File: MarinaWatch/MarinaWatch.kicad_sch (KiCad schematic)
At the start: 2 parts, among them J1 USB_C_Receptacle_USB2.0_16P, U1 ESP32-S3-WROOM-1

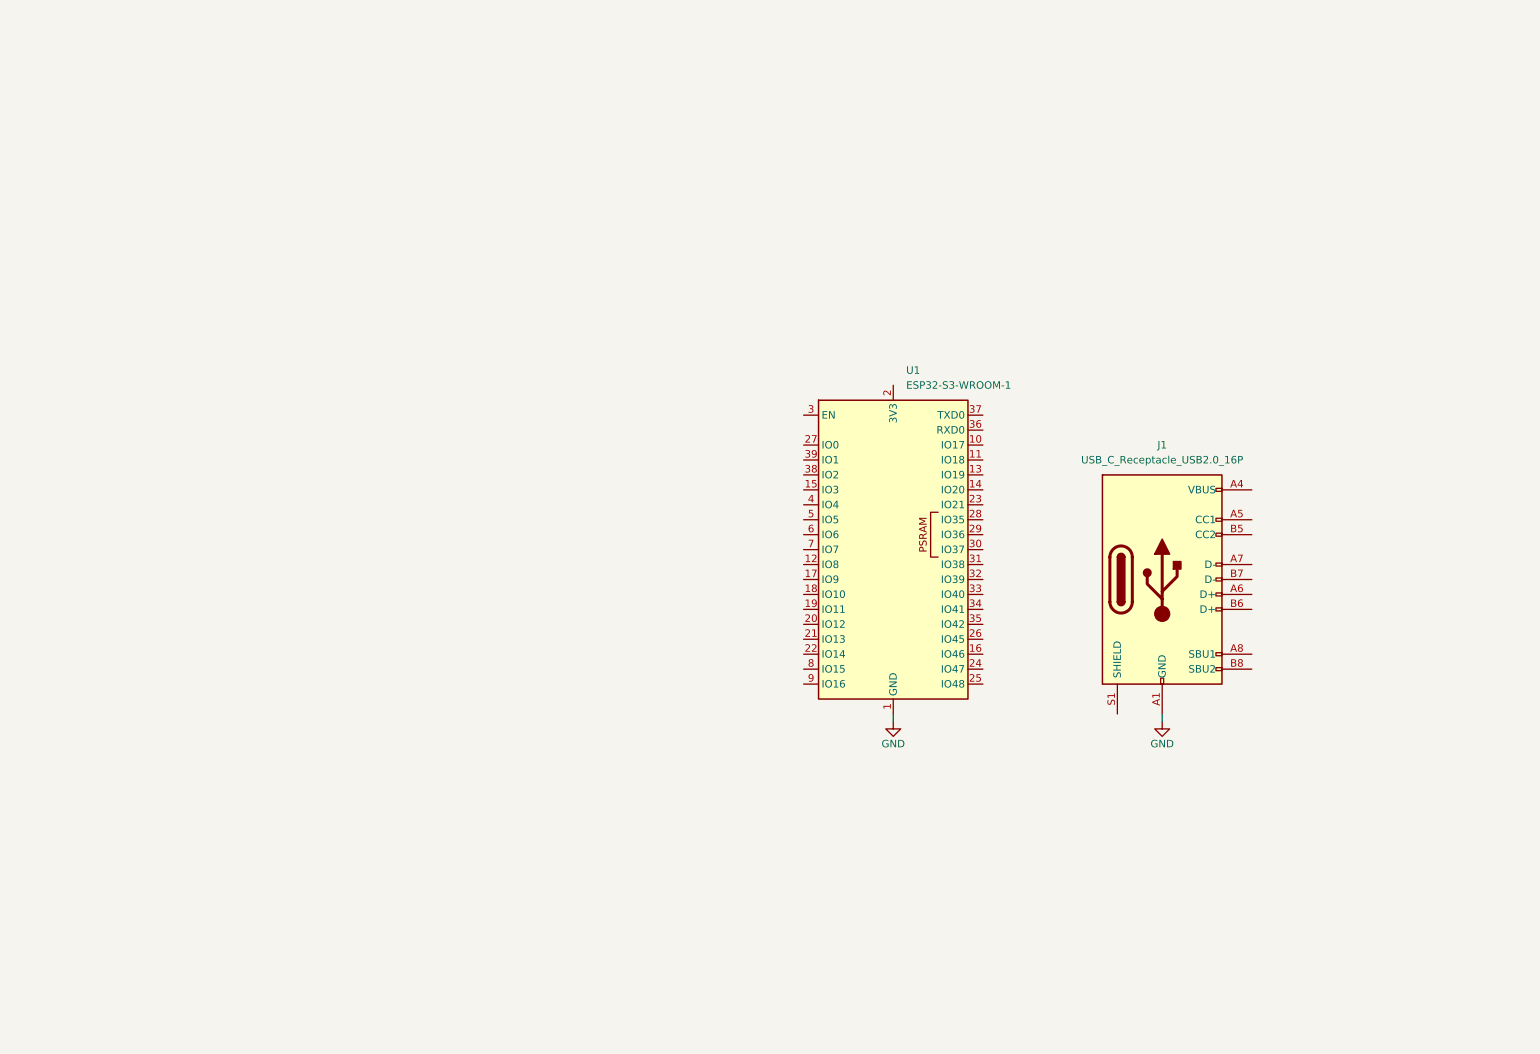
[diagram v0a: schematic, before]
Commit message: Finished USB hardware. Started power supply.
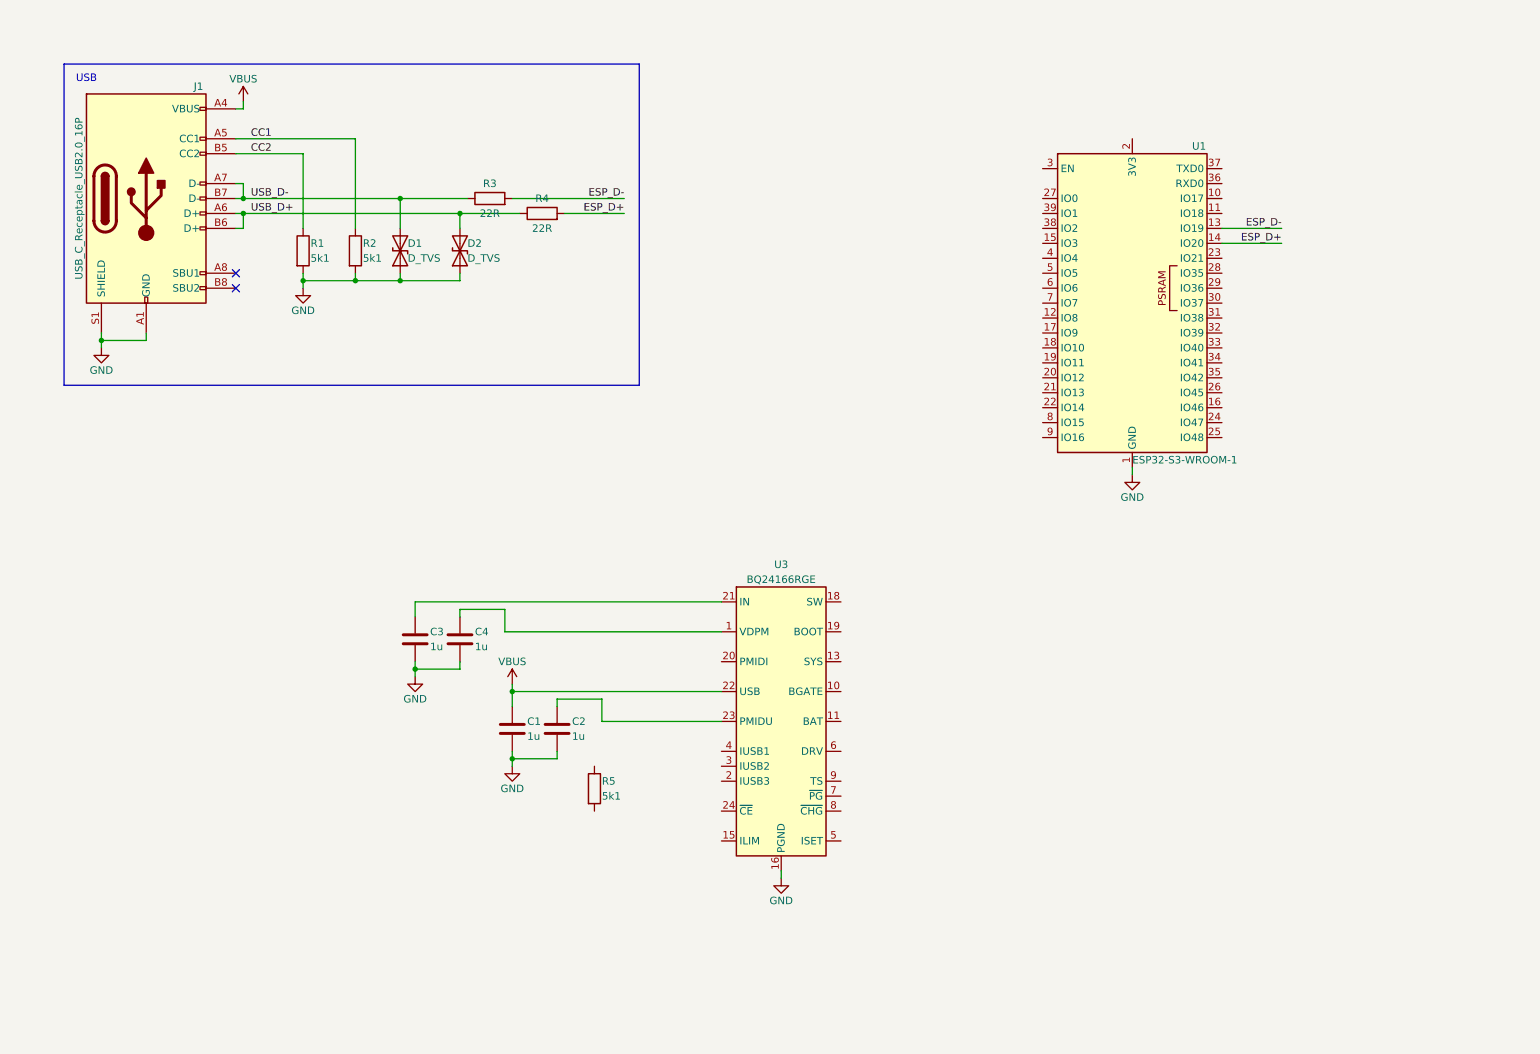
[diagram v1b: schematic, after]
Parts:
- added C1, C2, C3, C4: 1u, Capacitor_SMD:C_0603_1608Metric_Pad1.08x0.95mm_HandSolder, symbol Device:C
- added D1, D2: D_TVS, Fuse:Fuse_0603_1608Metric_Pad1.05x0.95mm_HandSolder, symbol Device:D_TVS
- added R1, R2, R5: 5k1, Resistor_SMD:R_0603_1608Metric_Pad0.98x0.95mm_HandSolder, symbol Device:R
- added R3, R4: 22R, Resistor_SMD:R_0603_1608Metric_Pad0.98x0.95mm_HandSolder, symbol Device:R
- added U3: BQ24166RGE, Package_DFN_QFN:Texas_RGE0024H_VQFN-24-1EP_4x4mm_P0.5mm_EP2.7x2.7mm, symbol Battery_Management:BQ24166RGE
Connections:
- net GND: now also J1.S1 (SHIELD), C1.2, C2.2, C3.2, C4.2, D1.1 (A1), D2.1 (A1), R1.2, R2.2, U3.16 (PGND), U3.17 (PGND), U3.25 (PGND)
- net VBUS: now reaches J1.A4 (VBUS), J1.A9 (VBUS), J1.B4 (VBUS), J1.B9 (VBUS)
- net VBUS: now also C1.1, U3.22 (USB)
- net CC1: now reaches J1.A5 (CC1)
- net CC1: now also R2.1
- net USB_D+: now reaches J1.A6 (D+)
- net USB_D+: now also J1.B6 (D+), D2.2 (A2), R4.1
- net USB_D-: now reaches J1.A7 (D-)
- net USB_D-: now also J1.B7 (D-), D1.2 (A2), R3.1
- net CC2: now reaches J1.B5 (CC2)
- net CC2: now also R1.1
- net ESP_D-: now reaches U1.13 (IO19)
- net ESP_D-: now also R3.2
- net ESP_D+: now reaches U1.14 (IO20)
- net ESP_D+: now also R4.2
- new net: C4.1, U3.1 (VDPM)
- new net: U3.11 (BAT), U3.12 (BAT)
- new net: U3.13 (SYS), U3.14 (SYS)
- new net: C3.1, U3.21 (IN)
- new net: C2.1, U3.23 (PMIDU)
- no-connect marks 0 -> 2
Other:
- note added: "USB"
- moved on the sheet: J1, U1

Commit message: Structure power supply chain
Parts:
- removed C4: 1u, Capacitor_SMD:C_0603_1608Metric_Pad1.08x0.95mm_HandSolder, symbol Device:C
- added BT1: Battery_Cell, symbol Device:Battery_Cell
- added C10, C11, C12: 10u, Capacitor_SMD:C_0603_1608Metric_Pad1.08x0.95mm_HandSolder, symbol Device:C
- added C5, C6, C7: 1u, Capacitor_SMD:C_0603_1608Metric_Pad1.08x0.95mm_HandSolder, symbol Device:C
- added C8: 4u7, Capacitor_SMD:C_0603_1608Metric_Pad1.08x0.95mm_HandSolder, symbol Device:C
- added C9: 100n, Capacitor_SMD:C_0603_1608Metric_Pad1.08x0.95mm_HandSolder, symbol Device:C
- added IC1: 2609011181000, Lund Formula Student:2609011181000, symbol Lund Formula Student:2609011181000
- added J2: Screw_Terminal_01x02, TerminalBlock_Phoenix:TerminalBlock_Phoenix_MKDS-3-2-5.08_1x02_P5.08mm_Horizontal, symbol Connector:Screw_Terminal_01x02
- added J3: Screw_Terminal_01x02, symbol Connector:Screw_Terminal_01x02
- added J4: Screw_Terminal_01x03, symbol Connector:Screw_Terminal_01x03
- added L1, L2: 2u2, Inductor_SMD_Wurth:L_Wurth_WE-LQSH-4020, symbol Device:L
- added R10: 1k, Resistor_SMD:R_0603_1608Metric_Pad0.98x0.95mm_HandSolder, symbol Device:R
- added R11: 100R, Resistor_SMD:R_0603_1608Metric_Pad0.98x0.95mm_HandSolder, symbol Device:R
- added R12, R6, R7, R8, R9: 10k, Resistor_SMD:R_0603_1608Metric_Pad0.98x0.95mm_HandSolder, symbol Device:R
- added R13: 27k, Resistor_SMD:R_0603_1608Metric_Pad0.98x0.95mm_HandSolder, symbol Device:R
- added TP1, TP2, TP3, TP4, TP5: TestPoint, TestPoint:TestPoint_Pad_D2.0mm, symbol Connector:TestPoint
- added U2: TPS63001, Package_SON:Texas_DRC0010J_ThermalVias, symbol Regulator_Switching:TPS63001
- R5: value 5k1 -> 10k
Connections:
- net GND: now also BT1.2 (-), C10.2, C11.2, C12.2, C5.2, C7.2, C8.2, C9.2, IC1.2 (GND_1), IC1.23 (GND_2), J2.2 (Pin_2), J3.2 (Pin_2), J4.3 (Pin_3), R10.2, R12.2, R6.2, R7.2, R8.2, R9.2, U2.11 (PGND), U2.3 (PGND), U2.9 (GND)
- net VBUS: now also R5.1, TP1.1
- net IUSB1: now reaches R5.2
- net IUSB1: now also U3.4 (IUSB1)
- net VDPM: now reaches U3.1 (VDPM)
- net VDPM: now also R12.1, R13.2
- net +BATT: now reaches U3.11 (BAT), U3.12 (BAT)
- net +BATT: now also BT1.1 (+), TP3.1
- net VCC: now reaches U3.13 (SYS), U3.14 (SYS)
- net VCC: now also C10.1, C7.1, L1.2, R11.1, TP4.1, U2.5 (VIN)
- net ILIM: now reaches U3.15 (ILIM)
- net ILIM: now also R8.1
- net SW: now reaches U3.18 (SW)
- net SW: now also C6.1, L1.1
- net BOOT: now reaches U3.19 (BOOT)
- net BOOT: now also C6.2
- net IUSB3: now reaches U3.2 (IUSB3)
- net IUSB3: now also R6.1
- net PMIDI: now reaches U3.20 (PMIDI)
- net PMIDI: now also C8.1
- net VDD: now reaches C3.1, U3.21 (IN)
- net VDD: now also J2.1 (Pin_1), R13.1, TP2.1
- net PMIDU: now reaches C2.1, U3.23 (PMIDU)
- net CE: now reaches U3.24 (~{CE})
- net CE: now also R9.1
- net IUSB2: now reaches U3.3 (IUSB2)
- net IUSB2: now also R7.1
- net ISET: now reaches U3.5 (ISET)
- net ISET: now also R10.1
- net DRV: now reaches U3.6 (DRV)
- net DRV: now also C5.1
- net +3.3V: now reaches U1.2 (3V3)
- net +3.3V: now also C11.1, C12.1, IC1.3 (VCC), J4.1 (Pin_1), TP5.1, U2.1 (VOUT), U2.10 (FB)
- new net ANALOG_TEMP: J3.1 (Pin_1)
- new net DIGITAL_TEMP: J4.2 (Pin_2)
- new net L1: L2.2, U2.4 (L1)
- new net L2: L2.1, U2.2 (L2)
- new net RF_RX: IC1.5 (URXD)
- new net RF_TX: IC1.4 (UTXD)
- new net VINA: C9.1, R11.2, U2.6 (EN), U2.7 (PS/SYNC), U2.8 (VINA)
- no-connect marks 2 -> 44
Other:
- note added: "INPUT POWER"
- note added: "R_ILIM = 251 AOhm / I_LIM R_ILIM = 251 / 0.025 = ~10k"
- note added: "R_ISET = 490 AOhm / I_SET R_ISET = 490 / 0.5 = ~1k"
- note added: "VOLTAGE REGULATOR"
- moved on the sheet: C1, C2, C3, D1, D2, J1, R1, R2, R3, R4, U1, U3

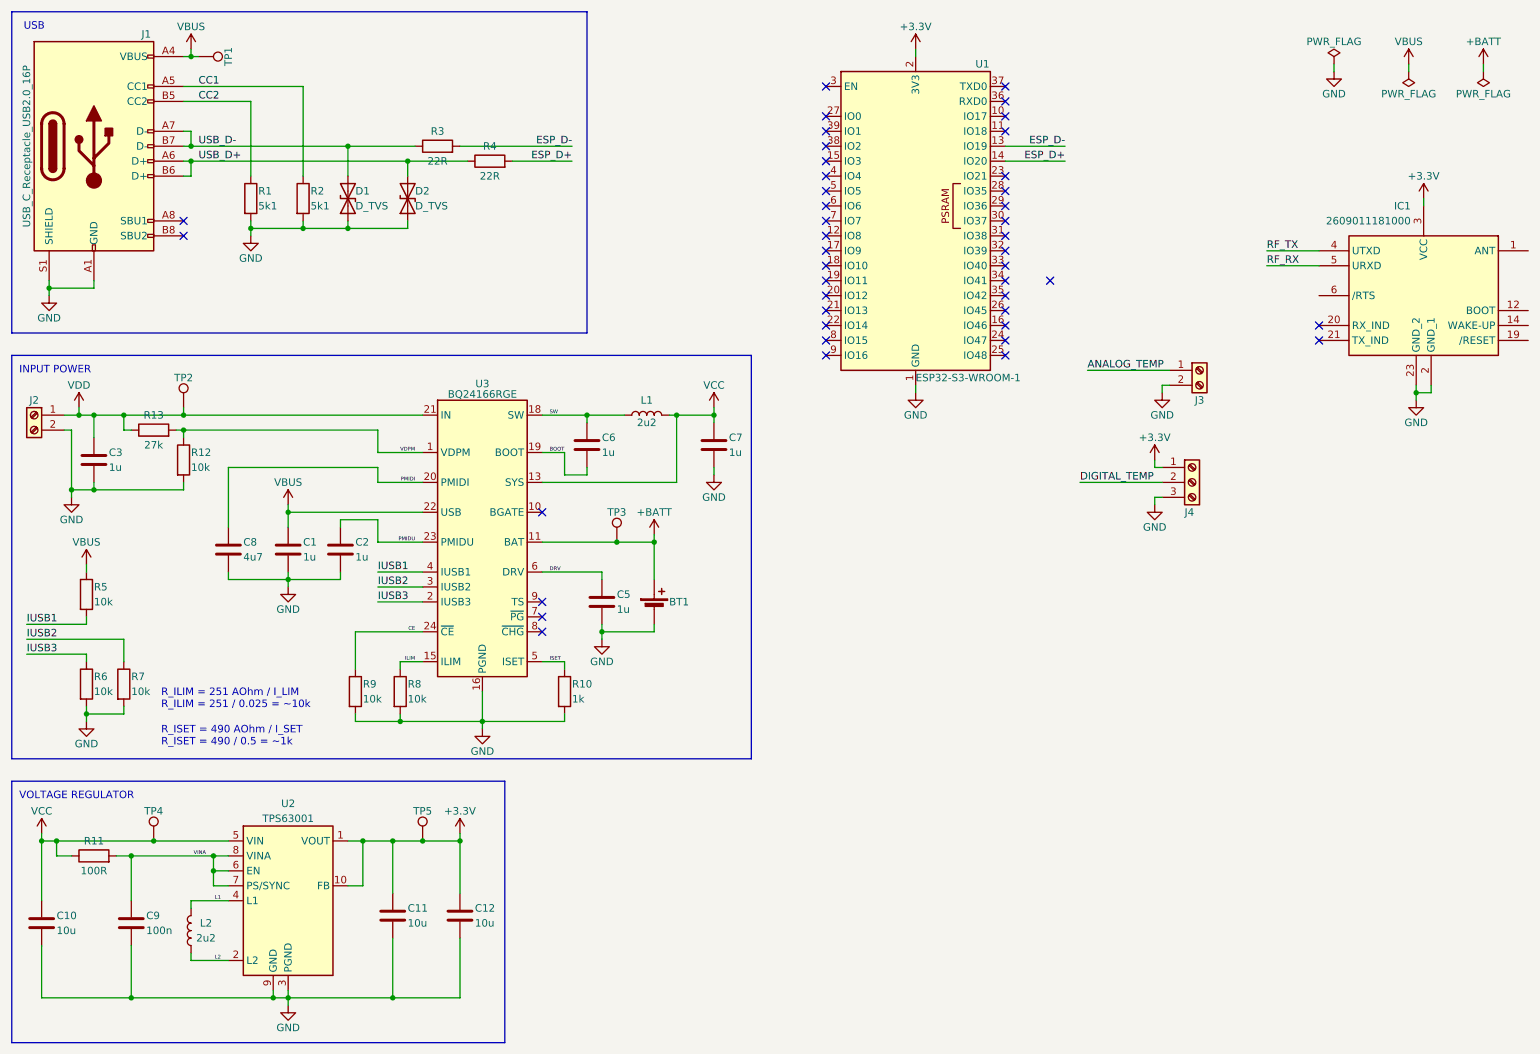
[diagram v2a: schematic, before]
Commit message: Restarted HW and started testing ESP32 WiFi
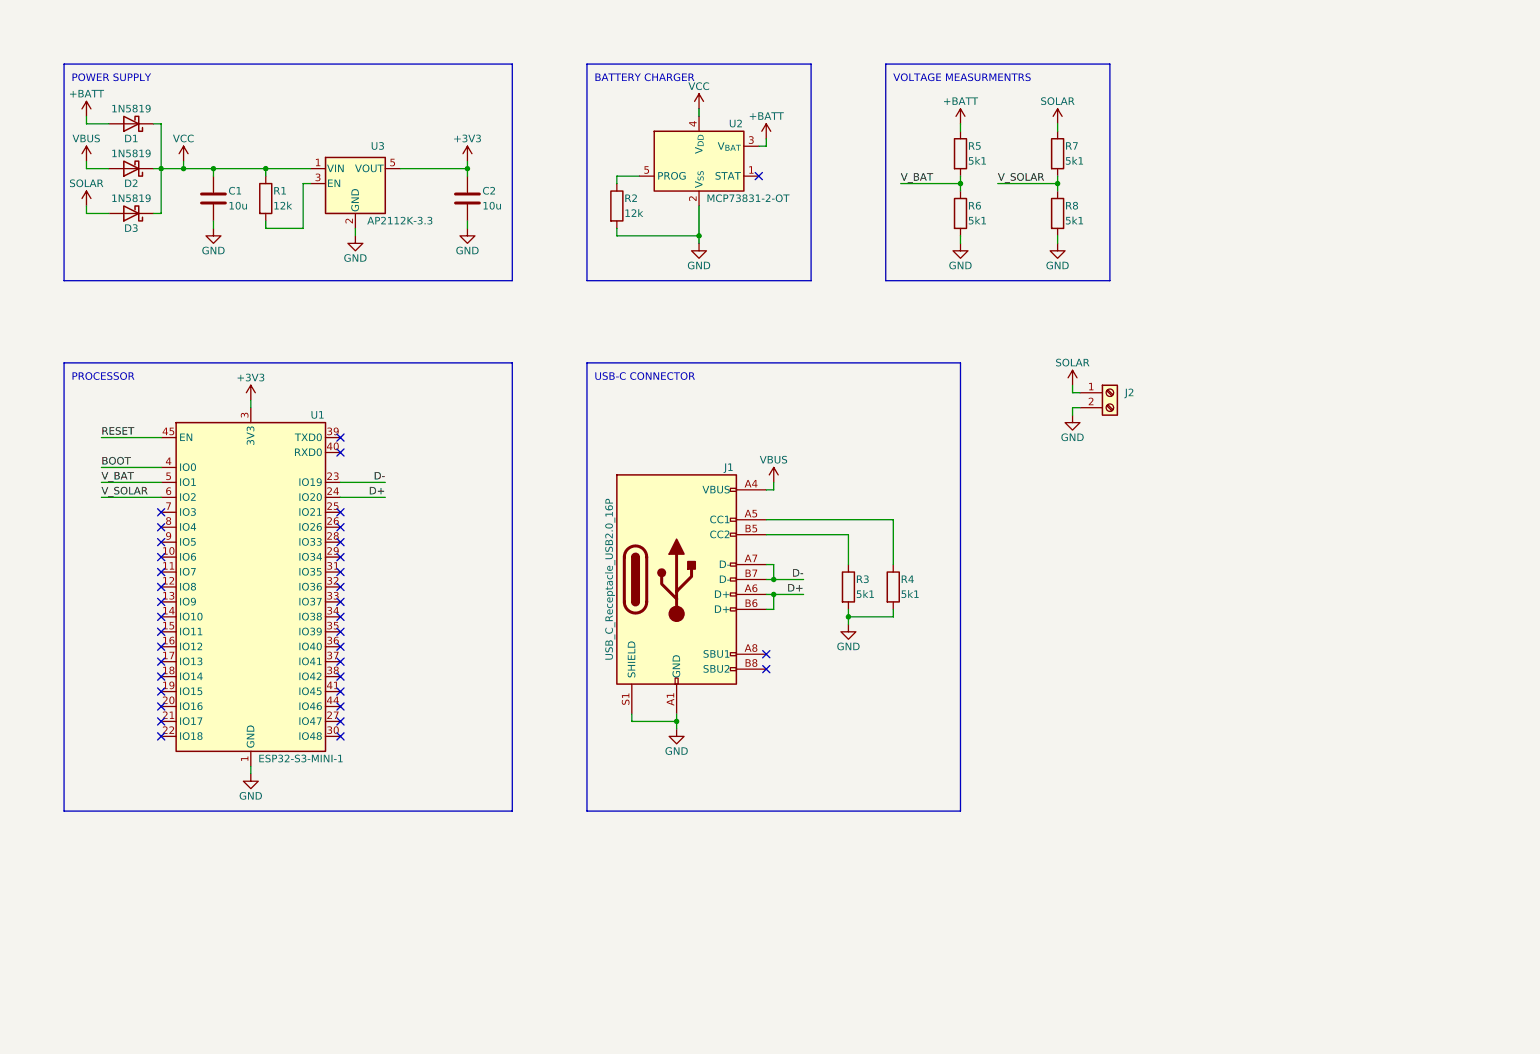
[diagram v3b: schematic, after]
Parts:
- removed BT1: Battery_Cell, symbol Device:Battery_Cell
- removed C10, C11, C12: 10u, Capacitor_SMD:C_0603_1608Metric_Pad1.08x0.95mm_HandSolder, symbol Device:C
- removed C3, C5, C6, C7: 1u, Capacitor_SMD:C_0603_1608Metric_Pad1.08x0.95mm_HandSolder, symbol Device:C
- removed C8: 4u7, Capacitor_SMD:C_0603_1608Metric_Pad1.08x0.95mm_HandSolder, symbol Device:C
- removed C9: 100n, Capacitor_SMD:C_0603_1608Metric_Pad1.08x0.95mm_HandSolder, symbol Device:C
- removed D1, D2: D_TVS, Fuse:Fuse_0603_1608Metric_Pad1.05x0.95mm_HandSolder, symbol Device:D_TVS
- removed IC1: 2609011181000, Lund Formula Student:2609011181000, symbol Lund Formula Student:2609011181000
- removed J3: Screw_Terminal_01x02, symbol Connector:Screw_Terminal_01x02
- removed J4: Screw_Terminal_01x03, symbol Connector:Screw_Terminal_01x03
- removed L1, L2: 2u2, Inductor_SMD_Wurth:L_Wurth_WE-LQSH-4020, symbol Device:L
- removed R10: 1k, Resistor_SMD:R_0603_1608Metric_Pad0.98x0.95mm_HandSolder, symbol Device:R
- removed R11: 100R, Resistor_SMD:R_0603_1608Metric_Pad0.98x0.95mm_HandSolder, symbol Device:R
- removed R12, R9: 10k, Resistor_SMD:R_0603_1608Metric_Pad0.98x0.95mm_HandSolder, symbol Device:R
- removed R13: 27k, Resistor_SMD:R_0603_1608Metric_Pad0.98x0.95mm_HandSolder, symbol Device:R
- removed TP1, TP2, TP3, TP4, TP5: TestPoint, TestPoint:TestPoint_Pad_D2.0mm, symbol Connector:TestPoint
- removed U1: ESP32-S3-WROOM-1, RF_Module:ESP32-S3-WROOM-1, symbol RF_Module:ESP32-S3-WROOM-1
- removed U2: TPS63001, Package_SON:Texas_DRC0010J_ThermalVias, symbol Regulator_Switching:TPS63001
- removed U3: BQ24166RGE, Package_DFN_QFN:Texas_RGE0024H_VQFN-24-1EP_4x4mm_P0.5mm_EP2.7x2.7mm, symbol Battery_Management:BQ24166RGE
- added D1, D2, D3: 1N5819, Diode_SMD:D_SOD-123, symbol Diode:1N5819
- added U1: ESP32-S3-MINI-1, RF_Module:ESP32-S2-MINI-1, symbol RF_Module:ESP32-S3-MINI-1
- added U2: MCP73831-2-OT, Package_TO_SOT_SMD:SOT-23-5, symbol Battery_Management:MCP73831-2-OT
- added U3: AP2112K-3.3, Package_TO_SOT_SMD:SOT-23-5, symbol Regulator_Linear:AP2112K-3.3
- C1, C2: value 1u -> 10u
- J2: footprint TerminalBlock_Phoenix:TerminalBlock_Phoenix_MKDS-3-2-5.08_1x02_P5.08mm_Horizontal -> TerminalBlock_MetzConnect:TerminalBlock_MetzConnect_Type101_RT01602HBWC_1x02_P5.08mm_Horizontal
- R1, R2: value 5k1 -> 12k
- R3, R4: value 22R -> 5k1
- R5, R6, R7, R8: value 10k -> 5k1
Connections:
- net ESP_D+ is gone; now on net GND: R4.2
- net ESP_D- is gone; now on net GND: R3.2
- net IUSB3 is gone; now on net V_BAT: R6.1
- net VDD is gone; now on net SOLAR: J2.1 (Pin_1)
- net +BATT: now also R5.1, D1.2 (A), U2.3 (V_{BAT})
- net BOOT: now also U1.4 (IO0)
- net GND: now also U1.1 (GND), U1.2 (GND), U1.42 (GND), U1.43 (GND), U1.46 (GND), U1.47 (GND), U1.48 (GND), U1.49 (GND), U1.50 (GND), U1.51 (GND), U1.52 (GND), U1.53 (GND), U1.54 (GND), U1.55 (GND), U1.56 (GND), U1.57 (GND), U1.58 (GND), U1.59 (GND), U1.60 (GND), U1.61 (GND), U1.62 (GND), U1.63 (GND), U1.64 (GND), U1.65 (GND), U2.2 (V_{SS}), U3.2 (GND); no longer R1.2, R7.2
- net VBUS: now also D2.2 (A); no longer C1.1, R5.1
- net VCC: now also C1.1, R1.1, D1.1 (K), D2.1 (K), D3.1 (K), U2.4 (V_{DD}), U3.1 (VIN)
- net CC1: no longer names the net of R2.1
- net CC1: now also U2.5 (PROG); no longer J1.A5 (CC1)
- net CC2: no longer names the net of J1.B5 (CC2)
- net CC2: now also R3.1; no longer R1.1
- net ILIM renamed V_SOLAR
- net V_SOLAR: now also R7.2, U1.6 (IO2)
- net IUSB1 renamed V_BAT
- net V_BAT: now also U1.5 (IO1)
- net IUSB2 renamed SOLAR
- net SOLAR: now also D3.2 (A)
- net PMIDU renamed +3V3
- net +3V3: now also U1.3 (3V3), U3.5 (VOUT)
- net USB_D+ renamed D+
- net D+: now also U1.24 (IO20); no longer R4.1
- net USB_D- renamed D-
- net D-: now also U1.23 (IO19); no longer R3.1
- new net: R1.2, U3.3 (EN)
- new net: J1.A5 (CC1), R4.1
- new net RESET: U1.45 (EN)
- no-connect marks 44 -> 37
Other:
- note added: "BATTERY CHARGER"
- note added: "POWER SUPPLY"
- note added: "PROCESSOR"
- note added: "USB-C CONNECTOR"
- note added: "VOLTAGE MEASURMENTRS"
- note removed: "INPUT POWER"
- note removed: "R_ILIM = 251 AOhm / I_LIM R_ILIM = 251 / 0.025 = ~10k"
- note removed: "R_ISET = 490 AOhm / I_SET R_ISET = 490 / 0.5 = ~1k"
- note removed: "USB"
- note removed: "VOLTAGE REGULATOR"
